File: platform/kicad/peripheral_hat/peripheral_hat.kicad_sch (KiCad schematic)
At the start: 25 parts, among them J1 CRJ032-1-TH, J2 Pi Header, T1 PT61018PEL, U2 ENC28J60x-SS, Y1 ABLS-25.000MHZ-20-A4-F-T

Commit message: Peripheral PCB: Finalise for production
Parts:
- removed Y1: ABLS-25.000MHZ-20-A4-F-T, AusOcean:XTAL_ABLS-25.000MHZ-20-A4-F-T, symbol AusOcean:ABLS-25.000MHZ-20-A4-F-T
- added X1: ~, AusOcean:X322525MOB4SI, symbol AusOcean:X322525MOB4SI
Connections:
- net at C16.2, R11.1, U2.24 (OSC2): now also X1.1
- net at C15.1, R11.2, U2.23 (OSC1): now also X1.3

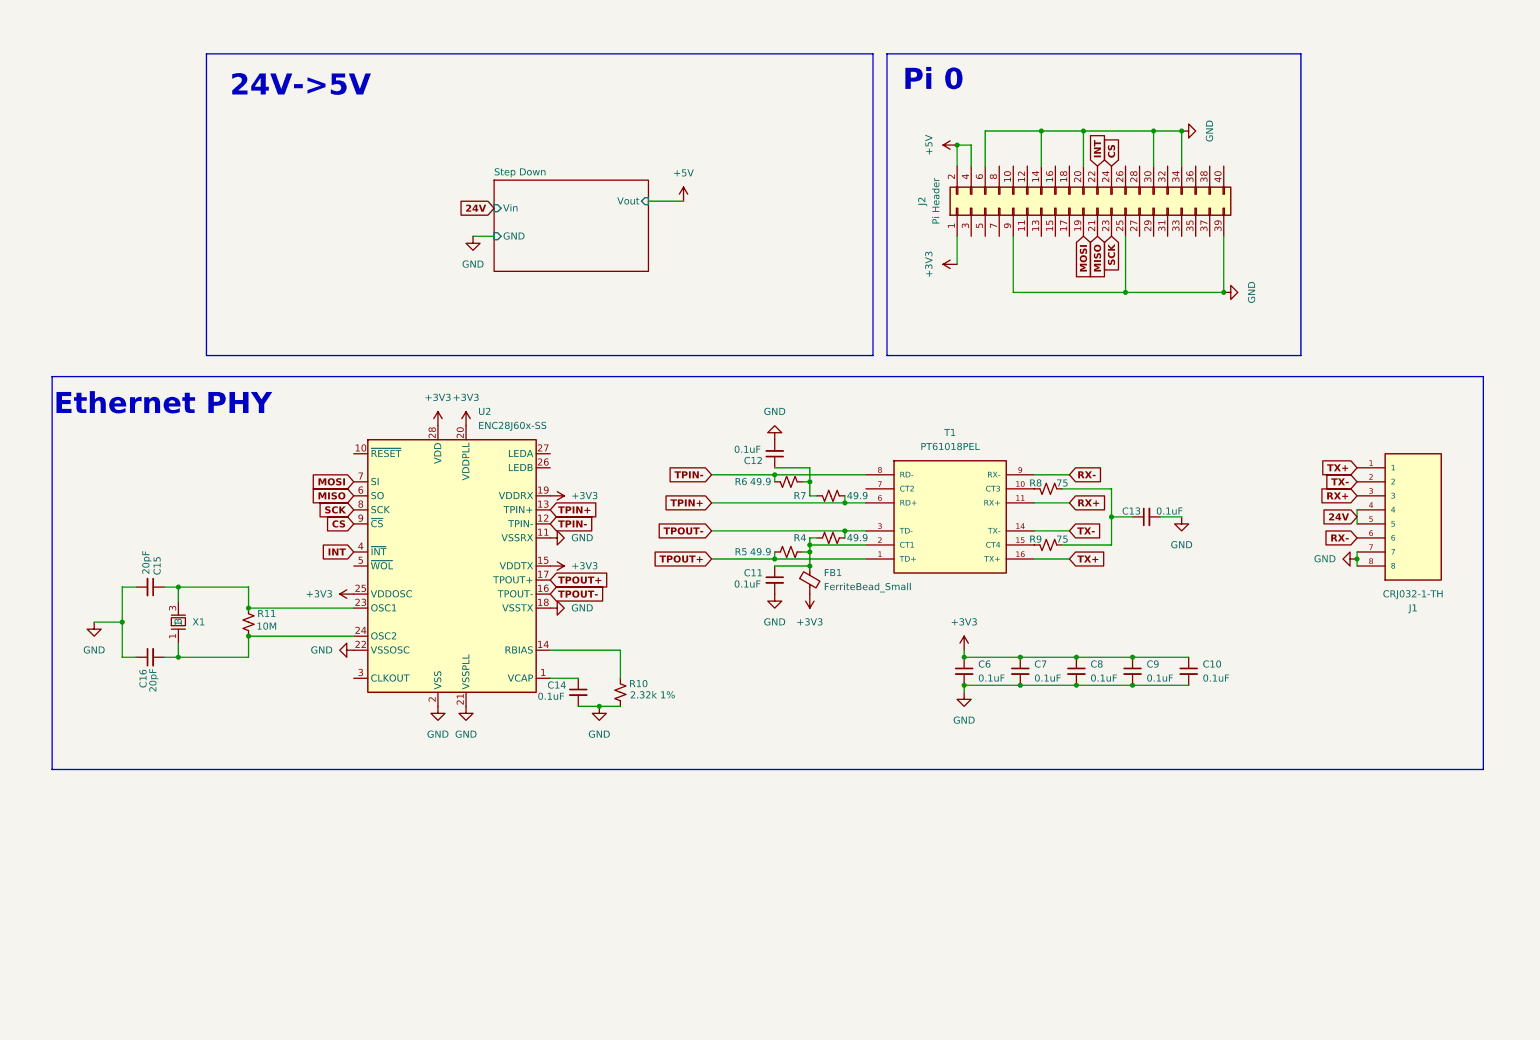
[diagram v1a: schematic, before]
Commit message: Controller: Finalise for production
This change updates the production files
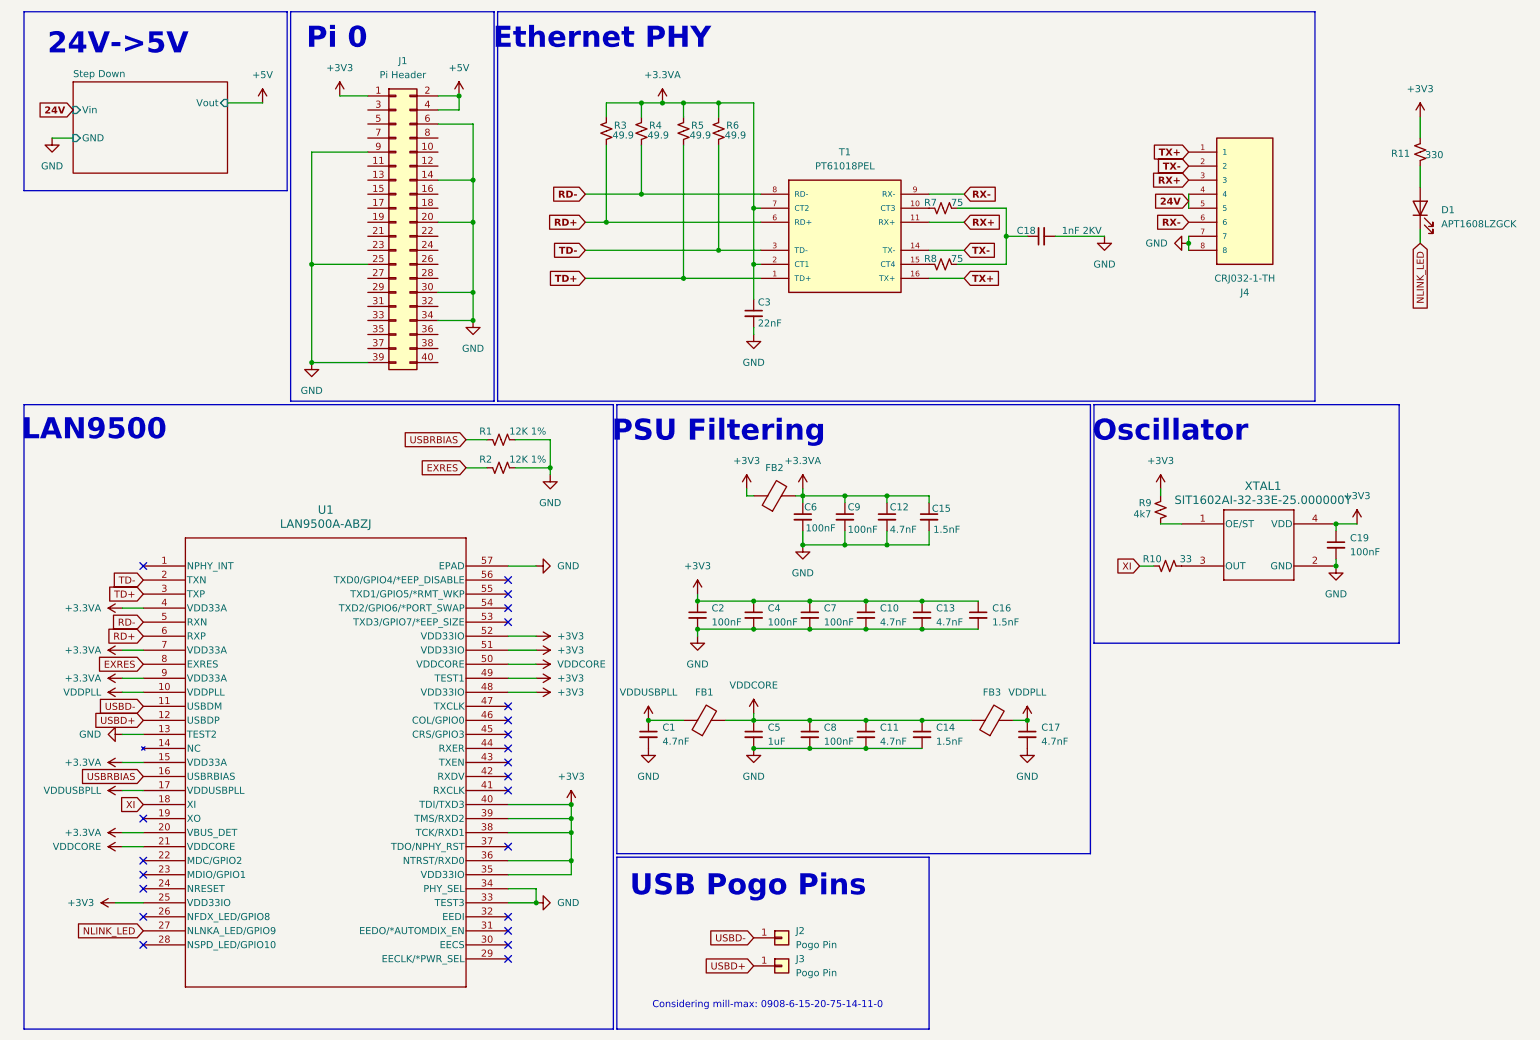
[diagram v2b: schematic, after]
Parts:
- removed C10: 0.1uF, Capacitor_SMD:C_0201_0603Metric, symbol Device:C_Small
- removed FB1: FerriteBead_Small, Resistor_SMD:R_0603_1608Metric, symbol Device:FerriteBead_Small
- removed R7: 49.9, Resistor_SMD:R_0201_0603Metric, symbol Device:R_Small_US
- removed U2: ENC28J60x-SS, Package_SO:SSOP-28_5.3x10.2mm_P0.65mm, symbol Interface_Ethernet:ENC28J60x-SS
- removed X1: ~, AusOcean:X322525MOB4SI, symbol AusOcean:X322525MOB4SI
- added C1, C11, C13, C17: 4.7nF, Capacitor_SMD:C_0402_1005Metric, symbol Device:C_Small
- added C19, C6, C8, C9: 100nF, Capacitor_SMD:C_0402_1005Metric, symbol Device:C_Small
- added C5: 1uF, Capacitor_SMD:C_0402_1005Metric, symbol Device:C_Small
- added D1: APT1608LZGCK, Capacitor_SMD:C_0805_2012Metric, symbol Device:LED
- added FB1, FB2, FB3: MMZ1608B121CTAH0, Capacitor_SMD:C_0603_1608Metric, symbol Device:FerriteBead
- added J2, J3: Pogo Pin, AusOcean:YZP0009-20130-01, symbol Connector_Generic:Conn_01x01
- added R1, R2: 12K 1%, Resistor_SMD:R_0402_1005Metric, symbol Device:R_Small_US
- added R3: 49.9, Resistor_SMD:R_0402_1005Metric, symbol Device:R_Small_US
- added R9: 4k7, Resistor_SMD:R_0402_1005Metric, symbol Device:R_Small_US
- added U1: LAN9500A-ABZJ, AusOcean:QFN56_8X8MC_MCH, symbol AusOcean:LAN9500A-ABZJ
- added XTAL1: SIT1602AI-32-33E-25.000000Y, AusOcean:SON4_SIT1602-3_SIT, symbol AusOcean:SIT1602AI-32-33E-25.000000Y
- C10: renamed from C9; value 0.1uF -> 4.7nF; footprint Capacitor_SMD:C_0201_0603Metric -> Capacitor_SMD:C_0402_1005Metric
- C12: value 0.1uF -> 4.7nF; footprint Capacitor_SMD:C_0201_0603Metric -> Capacitor_SMD:C_0402_1005Metric
- C14: value 0.1uF -> 1.5nF; footprint Capacitor_SMD:C_0201_0603Metric -> Capacitor_SMD:C_0402_1005Metric
- C15, C16: value 20pF -> 1.5nF; footprint Capacitor_SMD:C_0201_0603Metric -> Capacitor_SMD:C_0402_1005Metric
- C18: renamed from C13; value 0.1uF -> 1nF 2KV; footprint Capacitor_SMD:C_0201_0603Metric -> Capacitor_SMD:C_0402_1005Metric
- C2: renamed from C6; value 0.1uF -> 100nF; footprint Capacitor_SMD:C_0201_0603Metric -> Capacitor_SMD:C_0402_1005Metric
- C3: renamed from C11; value 0.1uF -> 22nF; footprint Capacitor_SMD:C_0201_0603Metric -> Capacitor_SMD:C_0402_1005Metric
- C4: renamed from C7; value 0.1uF -> 100nF; footprint Capacitor_SMD:C_0201_0603Metric -> Capacitor_SMD:C_0402_1005Metric
- C7: renamed from C8; value 0.1uF -> 100nF; footprint Capacitor_SMD:C_0201_0603Metric -> Capacitor_SMD:C_0402_1005Metric
- R10: value 2.32k 1% -> 33; footprint Resistor_SMD:R_0201_0603Metric -> Resistor_SMD:R_0402_1005Metric
- R11: value 10M -> 330; footprint Resistor_SMD:R_0201_0603Metric -> Resistor_SMD:R_0402_1005Metric
- R4, R5, R6: footprint Resistor_SMD:R_0201_0603Metric -> Resistor_SMD:R_0402_1005Metric
- R7: renamed from R8; footprint Resistor_SMD:R_0201_0603Metric -> Resistor_SMD:R_0402_1005Metric
- R8: renamed from R9; footprint Resistor_SMD:R_0201_0603Metric -> Resistor_SMD:R_0402_1005Metric
- renumbered J2 to J1, J1 to J4
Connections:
- net +3V3: now also C16.1, R11.2, C13.1, C19.1, FB2.1, R9.2, U1.25 (VDD33IO), U1.35 (VDD33IO), U1.36 (NTRST/RXD0), U1.38 (TCK/RXD1), U1.39 (TMS/RXD2), U1.40 (TDI/TXD3), U1.48 (VDD33IO), U1.49 (TEST1), U1.51 (VDD33IO), U1.52 (VDD33IO), XTAL1.4 (VDD)
- net GND: now also C16.2, C1.2, C11.2, C13.2, C17.2, C19.2, C5.2, C6.2, C8.2, C9.2, R1.1, R2.1, U1.13 (TEST2), U1.33 (TEST3), U1.34 (PHY_SEL), U1.57 (EPAD), XTAL1.2 (GND); no longer C16.1, R10.1
- net at R11.1: now also D1.2 (A); no longer C16.2
- net +3.3VA: now reaches C15.1
- net +3.3VA: now also C12.1, C3.1, R4.2, R5.2, R6.2, T1.2 (CT1), T1.7 (CT2), C6.1, C9.1, FB2.2, R3.2, U1.15 (VDD33A), U1.20 (VBUS_DET), U1.4 (VDD33A), U1.7 (VDD33A), U1.9 (VDD33A); no longer R11.2
- net VDDCORE: now reaches C14.1
- net VDDCORE: now also C11.1, C5.1, C8.1, FB1.2, FB3.1, U1.21 (VDDCORE), U1.50 (VDDCORE)
- net XI: now reaches R10.2
- net XI: now also U1.18 (XI)
- net CS: no longer names the net of J1.24 (Pin_24)
- net INT: no longer names the net of J1.22 (Pin_22)
- net MISO: no longer names the net of J1.21 (Pin_21)
- net MOSI: no longer names the net of J1.19 (Pin_19)
- net SCK: no longer names the net of J1.23 (Pin_23)
- net TPIN+ renamed RD+
- net RD+: now also R3.1, U1.6 (RXP)
- net TPIN- renamed RD-
- net RD-: now also R4.1, U1.5 (RXN); no longer R6.1
- net TPOUT+ renamed TD+
- net TD+: now also U1.3 (TXP)
- net TPOUT- renamed TD-
- net TD-: now also R6.1, U1.2 (TXN); no longer R4.2
- new net: R9.1, XTAL1.1 (OE/ST)
- new net: R10.1, XTAL1.3 (OUT)
- new net EXRES: R2.2, U1.8 (EXRES)
- new net NLINK_LED: D1.1 (K), U1.27 (NLNKA_LED/GPIO9)
- new net USBD+: J3.1 (Pin_1), U1.12 (USBDP)
- new net USBD-: J2.1 (Pin_1), U1.11 (USBDM)
- new net USBRBIAS: R1.2, U1.16 (USBRBIAS)
- new net VDDPLL: C17.1, FB3.2, U1.10 (VDDPLL)
- new net VDDUSBPLL: C1.1, FB1.1, U1.17 (VDDUSBPLL)
- no-connect marks 0 -> 23
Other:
- note added: "Considering mill-max: 0908-6-15-20-75-14-11-0"
- note added: "LAN9500"
- note added: "Oscillator"
- note added: "PSU Filtering"
- note added: "USB Pogo Pins"
- moved on the sheet: C10, C18, C2, C3, C4, C7, J1, J4, R7, R8, T1

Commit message: Pi Hat: Make review changes (#23)
This change makes the changes as recommended by the microchip review
service.
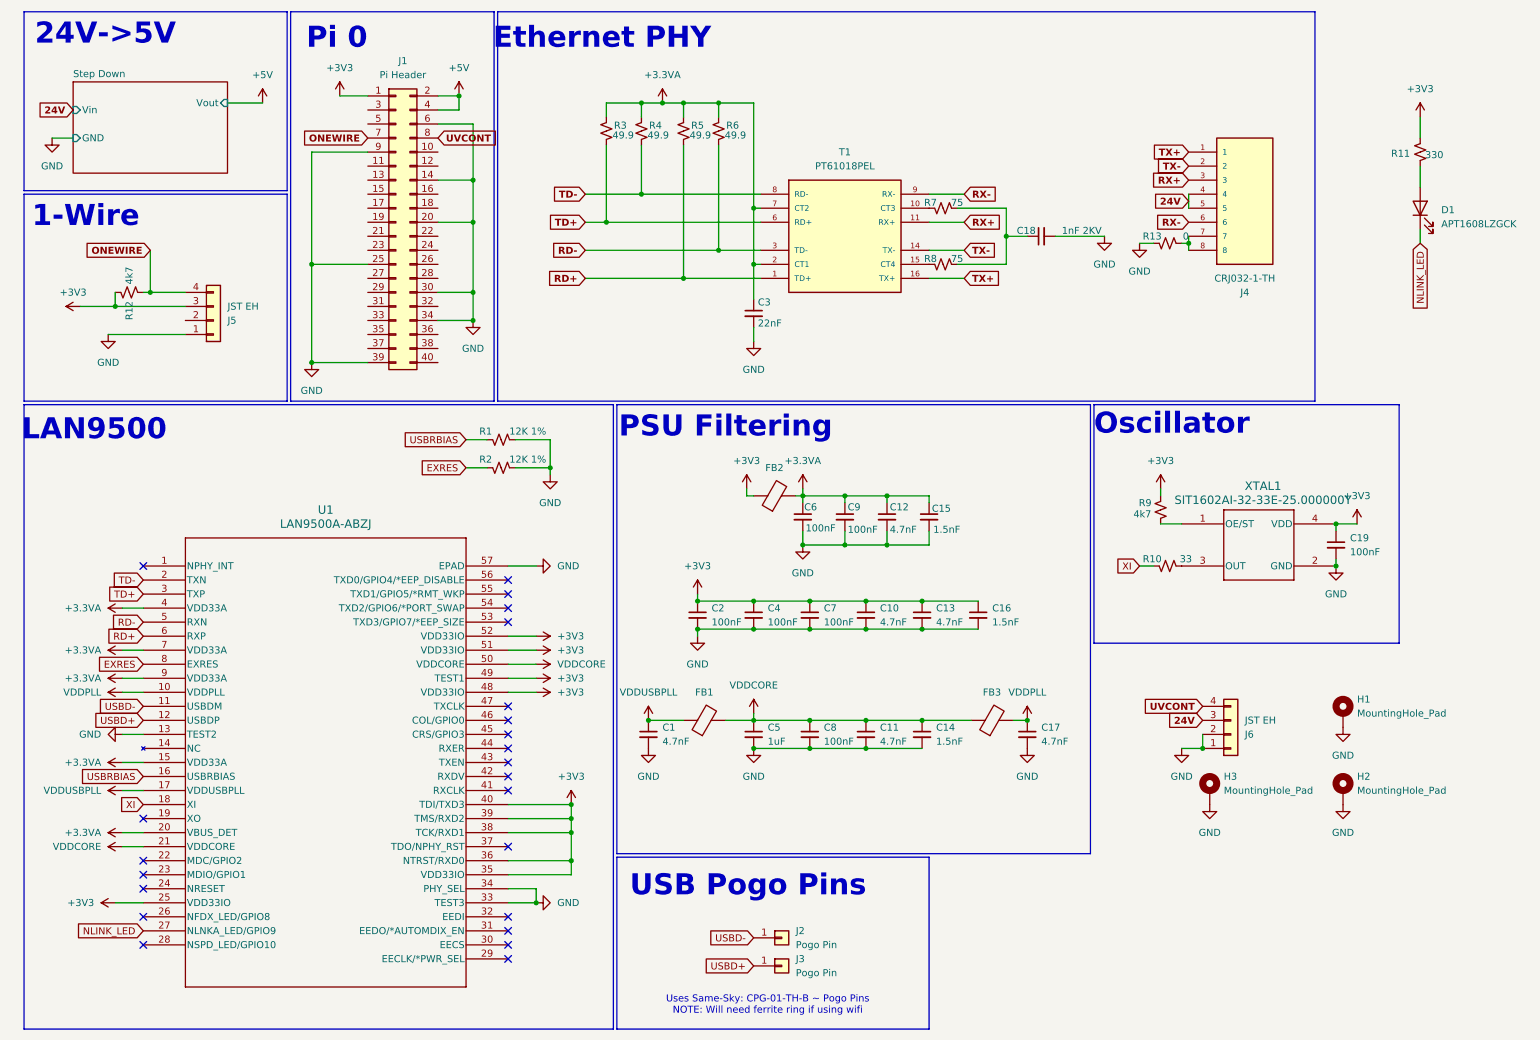
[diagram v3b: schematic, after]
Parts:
- added H1, H2, H3: MountingHole_Pad, MountingHole:MountingHole_2.7mm_M2.5_Pad_TopBottom, symbol Mechanical:MountingHole_Pad
- added J5, J6: JST EH, Connector_JST:JST_EH_B4B-EH-A_1x04_P2.50mm_Vertical, symbol Connector_Generic:Conn_01x04
- added R12: 4k7, Resistor_SMD:R_0402_1005Metric, symbol Device:R_Small_US
- added R13: 0, Resistor_SMD:R_0402_1005Metric, symbol Device:R_Small_US
- C1, C10, C12, C13, C15, C16, C4, C5, C6, C8, C9: footprint Capacitor_SMD:C_0402_1005Metric -> Capacitor_SMD:C_0201_0603Metric
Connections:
- net +3V3: now also J5.3 (Pin_3), R12.2
- net 24V: now also J6.3 (Pin_3)
- net GND: now also H1.1, H2.1, H3.1, J5.1 (Pin_1), J6.1 (Pin_1), J6.2 (Pin_2), R13.2; no longer J4.7, J4.8
- net RD+: now also R5.1, T1.1 (TD+); no longer R3.1, T1.6 (RD+)
- net RD-: now also R6.1, T1.3 (TD-); no longer R4.1, T1.8 (RD-)
- net TD+: now also R3.1, T1.6 (RD+); no longer R5.1, T1.1 (TD+)
- net TD-: now also R4.1, T1.8 (RD-); no longer R6.1, T1.3 (TD-)
- net ONEWIRE: now reaches J1.7 (Pin_7)
- net ONEWIRE: now also J5.4 (Pin_4), R12.1
- net UVCONT: now reaches J1.8 (Pin_8)
- net UVCONT: now also J6.4 (Pin_4)
- new net: J4.7, J4.8, R13.1
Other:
- note added: "1-Wire"
- note added: "Uses Same-Sky: CPG-01-TH-B ~ Pogo Pins NOTE: Will need ferrite ring if using wifi"
- note removed: "Considering mill-max: 0908-6-15-20-75-14-11-0"

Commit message: p_HAT: Clean up project files
This change just cleans up which files were being tracked and the
organisation of the files.
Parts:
- C18: footprint Capacitor_SMD:C_0402_1005Metric -> Capacitor_SMD:C_1206_3216Metric
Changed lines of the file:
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@@
 			)
 		)
-		(property "Footprint" "Capacitor_SMD:C_0402_1005Metric"
+		(property "Footprint" "Capacitor_SMD:C_1206_3216Metric"
 			(at 196.85 53.34 0)
 			(effects
